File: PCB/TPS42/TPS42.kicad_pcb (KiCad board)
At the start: 2 copper layers, 138.1 x 89.7 mm, 77 parts, among them J1 PJ-320A, J11 Conn_01x06, J14 FH12-10S-0.5SH, J3 TP Sensor Module, J4 TP Module, J6 OLED, J7 TrackPoint, J8 Battery, J9 TP Sensor Module, SW1 SW_DPST_x2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

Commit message: connect all mcu pins
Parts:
- added J5: Conn_01x02, Connector_PinHeader_2.54mm:PinHeader_1x02_P2.54mm_Vertical, F.Cu at (59.9, 49.0)
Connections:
- U1 pad 1: unconnected-(U1-Pad1) -> D3
- U1 pad 8: unconnected-(U1-Pad8) -> C6
- U14 pad 1: unconnected-(U14-Pad1) -> D3
- U14 pad 8: unconnected-(U14-Pad8) -> C6
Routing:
- net D3: track 0.00 -> 17.1 mm, vias 0 -> 1
- net C6: track 0.00 -> 15.8 mm, vias 0 -> 1
- net DAT: track 13.6 -> 24.9 mm, vias 1 -> 2
- net CLK: track 13.9 -> 23.4 mm, vias 1 -> 2
- net VCC: track 35.3 -> 44.7 mm, vias 1 -> 2
- net SERIAL: track 16.0 -> 19.3 mm, vias 1 -> 2
- net CS: track 14.8 -> 17.9 mm, vias 1 -> 2

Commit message: more routing
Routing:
- net COL2: track 72.9 -> 112.4 mm, vias 4 -> 6
- net COL1: track 39.0 -> 70.3 mm, vias 1 -> 3
- net Net-(D5-Pad2): track 31.8 -> 59.5 mm, vias 1 -> 2
- net ROW1: track 113.8 -> 141.3 mm, vias 5 -> 8
- net ROW0: track 131.3 -> 158.6 mm
- net Net-(D11-Pad2): track 34.9 -> 56.8 mm, vias 2 -> 3
- net Net-(D7-Pad2): track 10.0 -> 32.0 mm, vias 0 -> 1
- net COL4: track 130.6 -> 152.4 mm
- net Net-(D10-Pad2): track 34.2 -> 45.9 mm, vias 2 -> 3
- net Net-(D6-Pad2): track 8.44 -> 19.4 mm, vias 0 -> 1
- net ROW2: track 92.0 -> 95.5 mm

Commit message: and more routing
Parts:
- moved J1 74.7 mm to (23.6, 76.7), turned to 90 degrees
- moved J6 68.5 mm to (45.0, 83.9)
- moved J5 57.7 mm to (82.6, 102.1), turned to -150 degrees
- moved D4 0.52 mm to (96.5, 115.1)
- moved D13 0.12 mm to (179.5, 68.8)
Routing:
- net COL0: track 34.4 -> 131.3 mm, vias 1 -> 9
- net ROW3: track 25.5 -> 118.5 mm, vias 1 -> 8
- net COL5: track 119.7 -> 208.3 mm
- net COL2: track 112.4 -> 199.8 mm, vias 6 -> 9
- net TP_CLK: track 27.4 -> 105.8 mm, vias 2 -> 6
- net COL3: track 107.2 -> 172.2 mm, vias 4 -> 5
- net TP_DATA: track 22.8 -> 84.4 mm, vias 2 -> 3
- net COL1: track 70.3 -> 130.6 mm, vias 3 -> 4
- net COL4: track 152.4 -> 210.9 mm, vias 4 -> 6
- net ROW1: track 141.3 -> 189.3 mm, vias 8 -> 12
- net Net-(J8-Pad1): track 0.00 -> 44.9 mm, vias 0 -> 1
- net Net-(D12-Pad2): track 0.00 -> 38.2 mm, vias 0 -> 3
- net Net-(D4-Pad2): track 0.00 -> 36.5 mm, vias 0 -> 1
- net Net-(D8-Pad2): track 0.00 -> 35.1 mm, vias 0 -> 2
- net Net-(D6-Pad2): track 19.4 -> 43.5 mm, vias 1 -> 4
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
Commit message: and more routing
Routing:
- net ROW2: track 114.9 -> 271.8 mm, vias 6 -> 15
- net VCC: track 46.1 -> 133.8 mm, vias 3 -> 5
- net RESET: track 21.6 -> 106.1 mm, vias 2 -> 7
- net COL1: track 130.6 -> 200.0 mm, vias 4 -> 12
- net BAT+: track 33.8 -> 96.1 mm
- net C6: track 30.0 -> 83.4 mm, vias 1 -> 5
- net SERIAL: track 23.2 -> 74.2 mm
- net Net-(J8-Pad1): track 44.9 -> 88.7 mm, vias 1 -> 5
- net COL0: track 131.3 -> 169.1 mm, vias 9 -> 12
- net D3: track 30.0 -> 54.2 mm, vias 1 -> 2
- net GND: track 44.1 -> 65.5 mm
- net Net-(D3-Pad2): track 10.9 -> 31.7 mm, vias 0 -> 1
- net CLK: track 31.7 -> 48.8 mm, vias 2 -> 3
- net DAT: track 28.6 -> 39.5 mm
- net CS: track 24.4 -> 33.3 mm
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
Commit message: and even more routing
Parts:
- removed C2: 560pF/680pF, TPS42:C_0603_1608Metric_Pad1.08x0.95mm_HandSolder_Reversable
- removed C3, C4: 1uF, TPS42:C_0603_1608Metric_Pad1.08x0.95mm_HandSolder_Reversable
- removed FB1, FB2: Ferrite_Bead, Resistor_SMD:R_0805_2012Metric_Pad1.20x1.40mm_HandSolder
- removed J1: PJ-320A, TPS42:MJ-4PP-9
- removed J14: FH12-10S-0.5SH, Connector_FFC-FPC:Hirose_FH12-10S-0.5SH_1x10-1MP_P0.50mm_Horizontal
- removed J6: OLED, TPS42:OLED
- removed R6: 10kΩ, TPS42:R_0603_1608Metric_Pad0.98x0.95mm_HandSolder_Reversable
- removed U2, U3: Hole, TPS42:M2_HOLE_PCB
- moved SW1 1.53 mm to (85.5, 92.2)
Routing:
- net D3: track 54.2 -> 209.9 mm, vias 2 -> 9
- net DAT: track 39.5 -> 122.3 mm, vias 2 -> 4
- net CS: track 33.3 -> 73.4 mm, vias 2 -> 6
- net CLK: track 48.8 -> 75.3 mm, vias 3 -> 7
- net GND: track 65.5 -> 80.3 mm, vias 3 -> 80
- net COL1: track 200.0 -> 195.3 mm, vias 12 -> 11
- net Net-(D3-Pad2): track 31.7 -> 34.5 mm
- net Net-(D16-Pad2): track 42.6 -> 45.0 mm, vias 0 -> 1
- net ROW3: track 120.5 -> 122.7 mm
- net ROW2: track 271.8 -> 273.9 mm, vias 15 -> 16
- net Net-(J3-Pad3): track 53.5 -> 51.7 mm
- net ROW0: track 188.3 -> 189.8 mm, vias 12 -> 13
- net ROW1: track 194.9 -> 196.3 mm, vias 12 -> 13
- net Net-(J8-Pad1): track 88.7 -> 90.1 mm, vias 5 -> 3
- net RESET: track 106.1 -> 107.4 mm, vias 7 -> 8
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- added copper zone on B.Cu, net GND
- added copper zone on F.Cu, net GND

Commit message: finished main pcb routing
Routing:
- net GND: track 80.3 -> 104.9 mm, vias 80 -> 95
- net COL2: track 206.5 -> 207.3 mm
- net ROW0: track 189.8 -> 190.5 mm
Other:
- outline, holes or cut-outs redrawn
- board text added: "C6"
- board text added: "CS"
- board text added: "D3"
- board text added: "SER"
- board text added: "TPS42 Rev${Revision}"

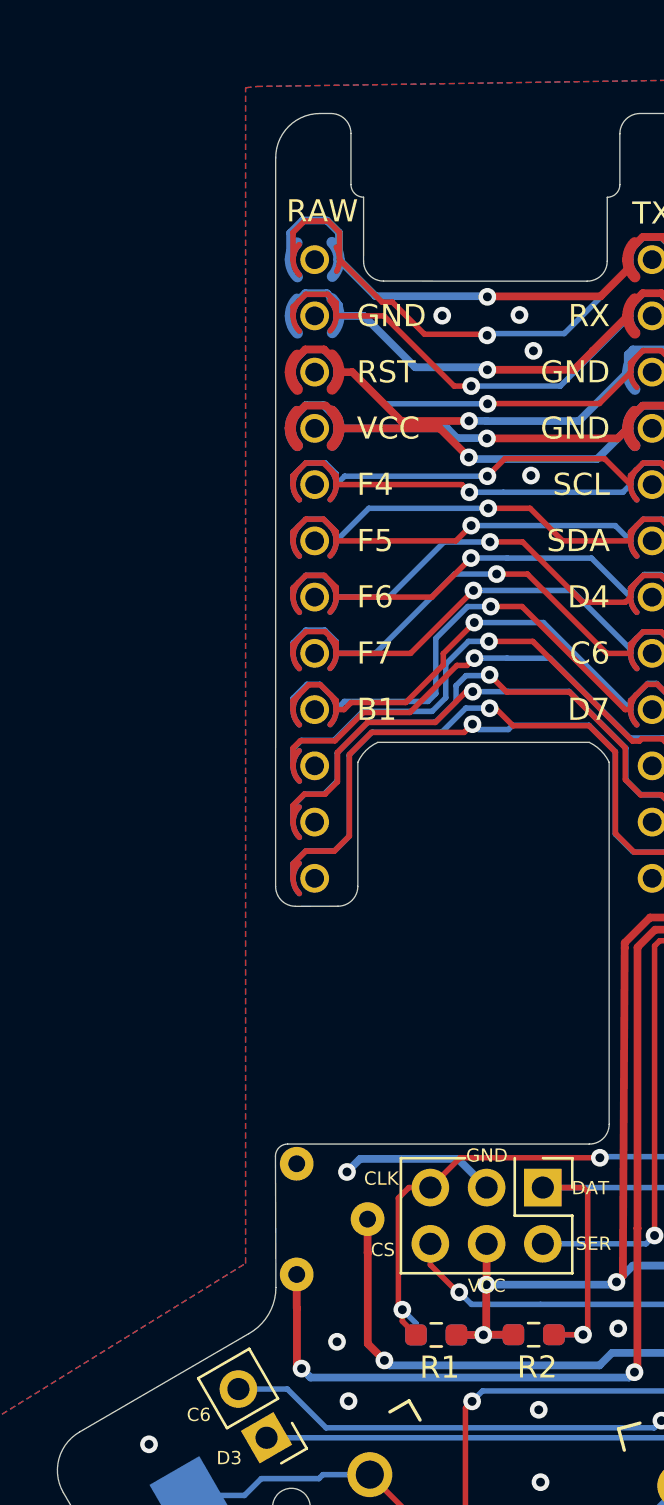
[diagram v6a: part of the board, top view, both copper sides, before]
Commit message: Added oled/trrs shield
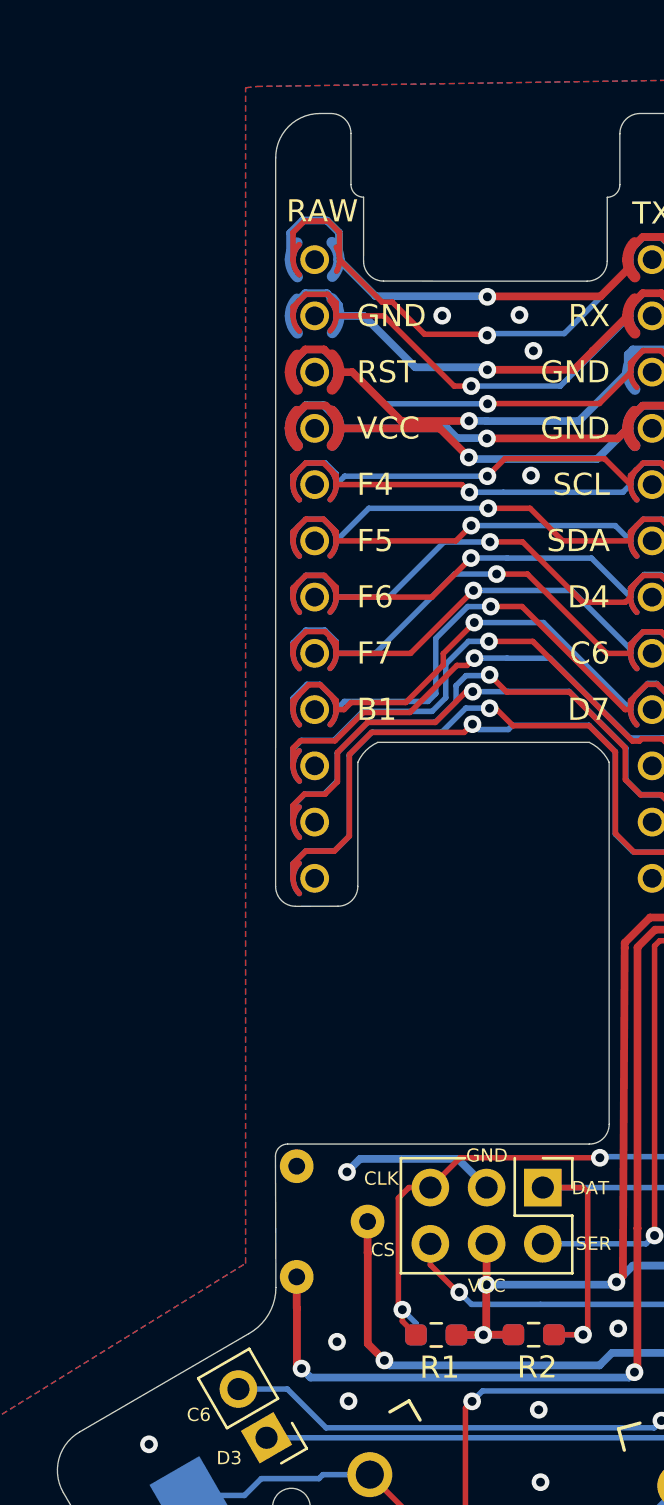
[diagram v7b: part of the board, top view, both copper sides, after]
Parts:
- moved SW1 0.11 mm to (85.5, 92.3)
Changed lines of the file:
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@@
   )
   (footprint "TPS42:SW-TH_3P-L9.1-W3.5-P2.50-S3.20-A3" (layer "B.Cu")
-    (at 85.54 92.18 90)
+    (at 85.54 92.29 90)
     (property "Sheetfile" "TPS42.kicad_sch")
     (property "Sheetname" "")
@@
   (gr_line (start 159.28 40.25) (end 173.275786 40.244214) (layer "Edge.Cuts") (width 0.05))
   (gr_arc (start 192.765494 88.07) (mid 191.363961 86.24) (end 192.765494 84.41) (layer "Edge.Cuts") (width 0.05))
-  (gr_line (start 86.39 43.16) (end 86.39 45.46) (layer "Edge.Cuts") (width 0.05))
+  (gr_line (start 86.39 43.150001) (end 86.39 45.46) (layer "Edge.Cuts") (width 0.05))
   (gr_line (start 84.990001 42.250001) (end 85.49 42.250001) (layer "Edge.Cuts") (width 0.05))
   (gr_line (start 138.535685 93.23) (end 174.474315 93.23) (layer "Edge.Cuts") (width 0.05))
@@
     (effects (font (size 0.6 0.6) (thickness 0.1)))
   )
-  (gr_text "D3" (at 80.89 102.97) (layer "F.SilkS")
-    (effects (font (size 0.6 0.6) (thickness 0.1)))
-  )
   (gr_text "4" (at 155.2 89.63) (layer "F.SilkS")
     (effects (font (size 1 1) (thickness 0.15)))
@@
   )
   (gr_text "DAT" (at 134.25 94.68 90) (layer "F.SilkS")
+    (effects (font (size 0.6 0.6) (thickness 0.1)))
+  )
+  (gr_text "D3" (at 80.89 102.97) (layer "F.SilkS")
     (effects (font (size 0.6 0.6) (thickness 0.1)))
   )
@@
   (via (at 106 52.64) (size 0.8) (drill 0.4) (layers "F.Cu" "B.Cu") (free) (net 28))
   (via (at 107.27 59.85) (size 0.8) (drill 0.4) (layers "F.Cu" "B.Cu") (free) (net 28))
+  (via (at 94.52 58.6) (size 0.8) (drill 0.4) (layers "F.Cu" "B.Cu") (free) (net 28))
   (via (at 143.02 52.24) (size 0.8) (drill 0.4) (layers "F.Cu" "B.Cu") (free) (net 28))
   (via (at 132.99 60.53) (size 0.8) (drill 0.4) (layers "F.Cu" "B.Cu") (free) (net 28))
@@
   (via (at 143.03 88.18) (size 0.8) (drill 0.4) (layers "F.Cu" "B.Cu") (free) (net 28))
   (via (at 115.84 100.69) (size 0.8) (drill 0.4) (layers "F.Cu" "B.Cu") (free) (net 28))
-  (via (at 94.52 58.6) (size 0.8) (drill 0.4) (layers "F.Cu" "B.Cu") (free) (net 28))
   (via (at 139.84 67.54) (size 0.8) (drill 0.4) (layers "F.Cu" "B.Cu") (free) (net 28))
   (via (at 86.21 90.05) (size 0.8) (drill 0.4) (layers "F.Cu" "B.Cu") (free) (net 28))
@@
   (segment (start 122.23 90.4) (end 122.23 94.89) (width 0.35) (layer "F.Cu") (net 32))
   (segment (start 122.23 94.89) (end 121.9 95.22) (width 0.35) (layer "F.Cu") (net 32))
-  (segment (start 87.14 93.7) (end 87.14 92.18) (width 0.35) (layer "F.Cu") (net 32))
+  (segment (start 87.9 98.56) (end 87.15 97.81) (width 0.35) (layer "F.Cu") (net 32))
+  (segment (start 87.14 93.7) (end 87.14 92.29) (width 0.35) (layer "F.Cu") (net 32))
+  (segment (start 87.15 93.71) (end 87.14 93.7) (width 0.35) (layer "F.Cu") (net 32))
   (segment (start 87.15 97.81) (end 87.15 93.71) (width 0.35) (layer "F.Cu") (net 32))
-  (segment (start 87.9 98.56) (end 87.15 97.81) (width 0.35) (layer "F.Cu") (net 32))
-  (segment (start 87.15 93.71) (end 87.14 93.7) (width 0.35) (layer "F.Cu") (net 32))
   (via (at 87.9 98.56) (size 0.8) (drill 0.4) (layers "F.Cu" "B.Cu") (net 32))
   (via (at 122.23 90.4) (size 0.8) (drill 0.4) (layers "F.Cu" "B.Cu") (net 32))
@@
   (segment (start 101.895 75.18) (end 110.87 75.18) (width 0.25) (layer "B.Cu") (net 40))
   (segment (start 187.20952 76.53952) (end 198.84048 76.53952) (width 0.25) (layer "B.Cu") (net 40))
-  (segment (start 83.94 96.2) (end 83.94 94.68) (width 0.35) (layer "F.Cu") (net 41))
+  (segment (start 83.94 96.2) (end 83.94 94.79) (width 0.35) (layer "F.Cu") (net 41))
   (segment (start 101.732943 79.10952) (end 100.124052 79.10952) (width 0.35) (layer "F.Cu") (net 41))
   (segment (start 98.89 49.28) (end 98.89 48.85) (width 0.35) (layer "F.Cu") (net 41))
+  (segment (start 83.95 96.21) (end 83.94 96.2) (width 0.35) (layer "F.Cu") (net 41))
   (segment (start 99.33 79.903572) (end 99.33 92.594675) (width 0.35) (layer "F.Cu") (net 41))
-  (segment (start 83.95 98.72) (end 84.16 98.93) (width 0.35) (layer "F.Cu") (net 41))
   (segment (start 98.89 48.501122) (end 99.565633 47.825489) (width 0.35) (layer "F.Cu") (net 41))
   (segment (start 99.193062 99.092734) (end 99.3 99.04) (width 0.35) (layer "F.Cu") (net 41))
   (segment (start 99.325489 92.599186) (end 99.325489 98.960307) (width 0.35) (layer "F.Cu") (net 41))
   (segment (start 100.455489 47.825489) (end 101.09 48.46) (width 0.35) (layer "F.Cu") (net 41))
-  (segment (start 83.95 96.21) (end 83.95 98.72) (width 0.35) (layer "F.Cu") (net 41))
   (segment (start 99.325489 98.960307) (end 99.193062 99.092734) (width 0.35) (layer "F.Cu") (net 41))
   (segment (start 101.09 48.46) (end 101.09 48.85) (width 0.35) (layer "F.Cu") (net 41))
   (segment (start 92.57 50.51) (end 97.66 50.51) (width 0.35) (layer "F.Cu") (net 41))
   (segment (start 99.33 92.594675) (end 99.325489 92.599186) (width 0.35) (layer "F.Cu") (net 41))
-  (segment (start 83.95 96.21) (end 83.94 96.2) (width 0.35) (layer "F.Cu") (net 41))
+  (segment (start 84.16 98.93) (end 83.95 98.72) (width 0.35) (layer "F.Cu") (net 41))
   (segment (start 99.565633 47.825489) (end 100.455489 47.825489) (width 0.35) (layer "F.Cu") (net 41))
+  (segment (start 83.95 98.72) (end 83.95 96.21) (width 0.35) (layer "F.Cu") (net 41))
   (segment (start 103.134031 50.894031) (end 103.13403 77.708433) (width 0.35) (layer "F.Cu") (net 41))
   (segment (start 103.13403 77.708433) (end 101.732943 79.10952) (width 0.35) (layer "F.Cu") (net 41))

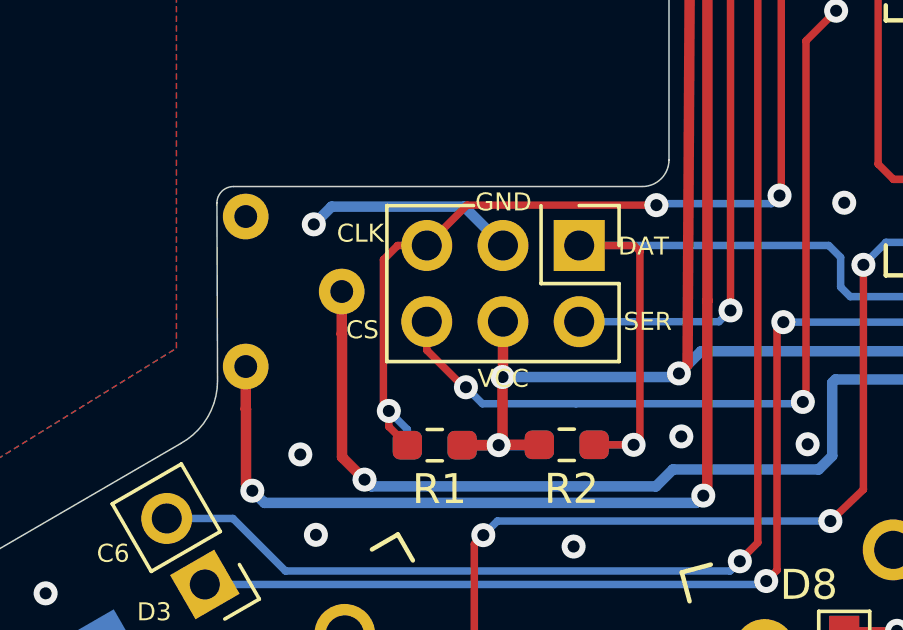
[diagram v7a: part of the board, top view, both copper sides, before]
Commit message: center shield pins with mcu
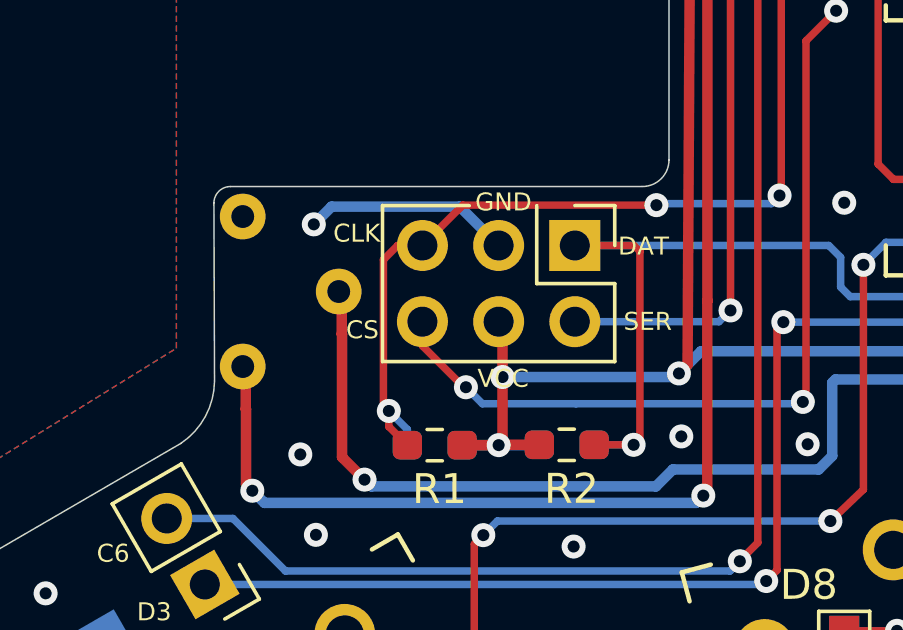
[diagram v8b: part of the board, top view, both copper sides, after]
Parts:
- moved J11 0.15 mm to (94.9, 90.8)
- moved SW1 0.10 mm to (85.4, 92.3)
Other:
- outline, holes or cut-outs redrawn
